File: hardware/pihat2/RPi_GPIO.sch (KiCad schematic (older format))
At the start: 1 part, among them J2 RPi_GPIO

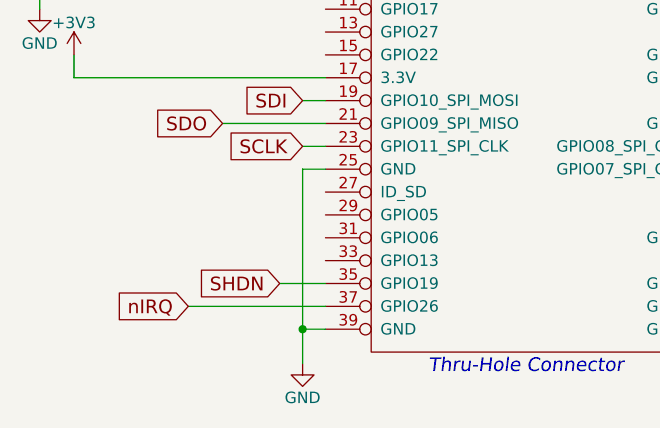
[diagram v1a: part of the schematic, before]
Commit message: Fixed issues with grounding and trace size.
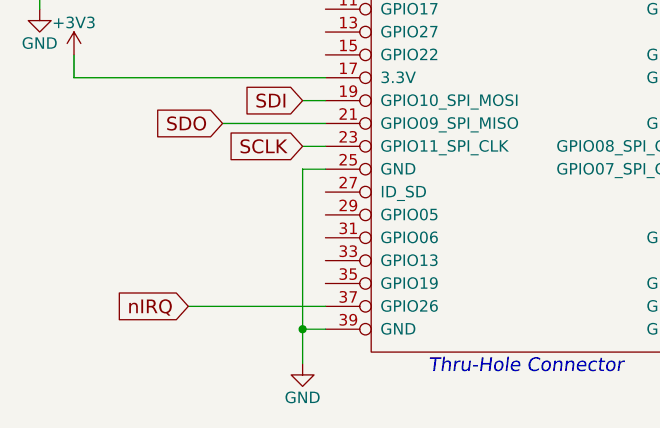
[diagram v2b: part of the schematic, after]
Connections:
- net SHDN: no longer names the net of J2.35 (GPIO19)
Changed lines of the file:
@@
 LIBS:contrib
 LIBS:valves
+LIBS:RFT
 LIBS:RPi_Hat-cache
 EELAYER 25 0
@@
 Wire Wire Line
 	1200 2800 1800 2800
-Wire Wire Line
-	1800 2700 1600 2700
-Text GLabel 1600 2700 0    60   Input ~ 0
-SHDN
 Text GLabel 1200 2800 0    60   Input ~ 0
 nIRQ
